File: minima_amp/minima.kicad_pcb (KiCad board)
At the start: 2 copper layers, 78 x 60 mm, 40 parts, among them J1 input, J2 output, J3 powersupply, U1 LM1875

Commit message: Minor PCB adjustements
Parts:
- moved J1 0.64 mm to (120.6, 97.7)
- moved J3 0.08 mm to (140.6, 99.8)
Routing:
- net VCC: track 50.4 -> 46.4 mm
- net GNDPWR: track 106.8 -> 102.9 mm
- net VEE: track 53.5 -> 49.6 mm
- net /inp: track 13.4 -> 12.5 mm
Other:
- board text added: "180801"
- board text added: "Grid alignements: - Components: PIN3 (U1) 25mil - Planes: PIN4 (U1) 10mil - Connectors: LEFT-UP Corner 1mm"
- board text removed: "20180801"

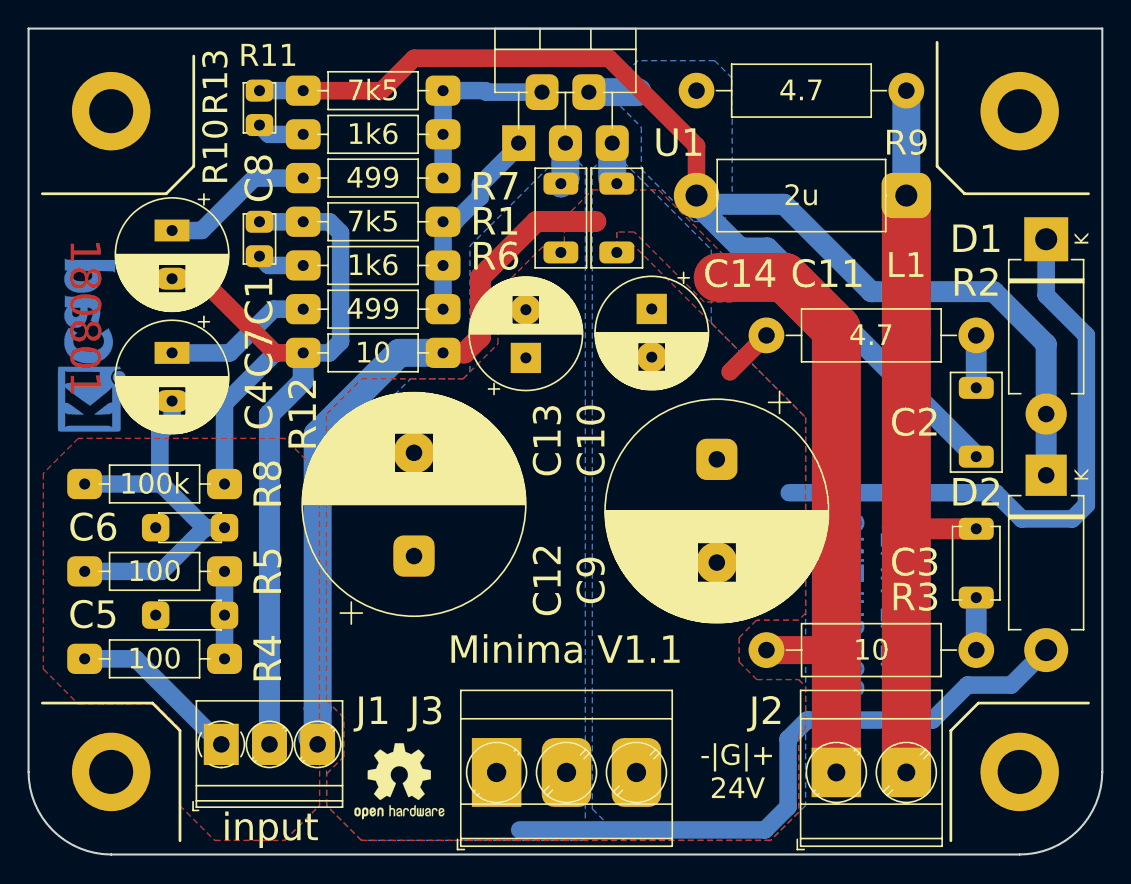
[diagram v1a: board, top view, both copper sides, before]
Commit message: Using designators as specified in README.rst
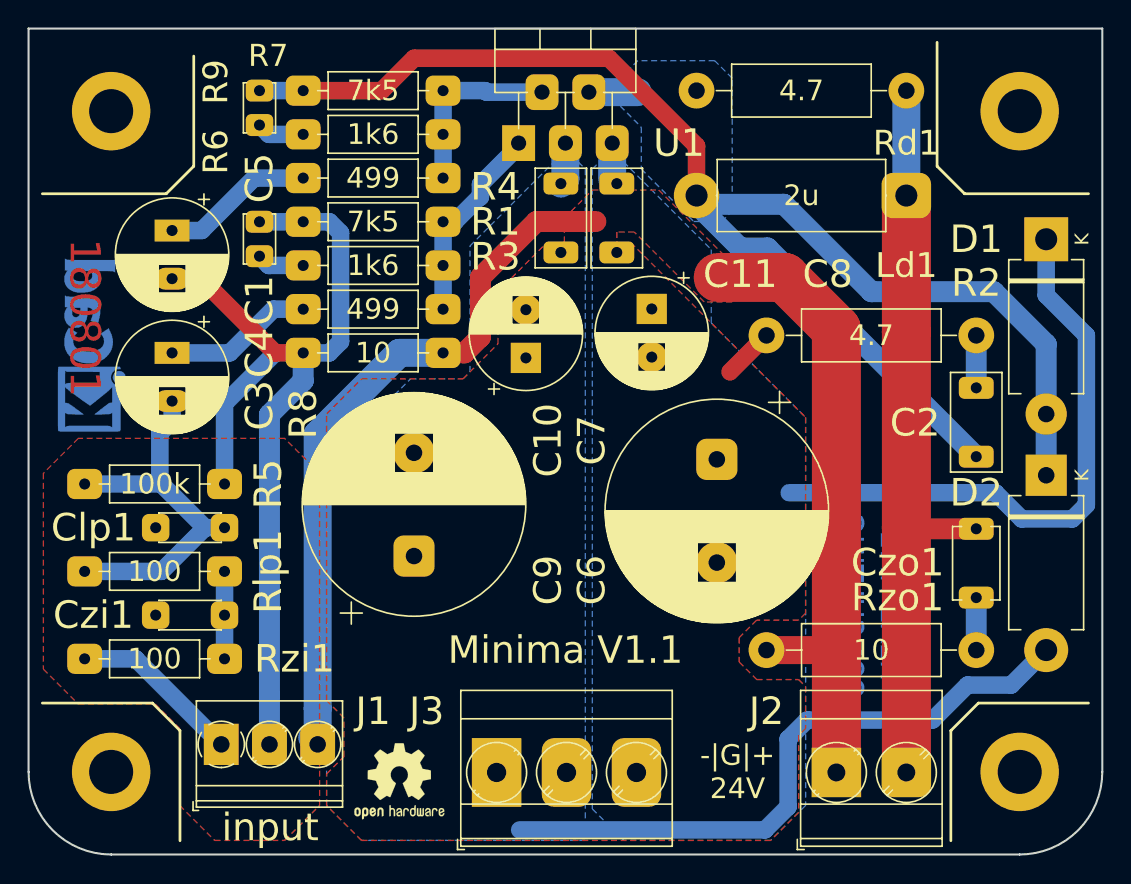
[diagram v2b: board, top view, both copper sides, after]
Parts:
- renumbered C13 to C10, C14 to C11, C4 to C3, C7 to C4, C8 to C5, C9 to C6, C10 to C7, C11 to C8, C12 to C9, C6 to Clp1, C5 to Czi1, C3 to Czo1, L1 to Ld1, R6 to R3, R7 to R4, R8 to R5, R10 to R6, R11 to R7, R12 to R8, R13 to R9, R9 to Rd1, R5 to Rlp1, R4 to Rzi1, R3 to Rzo1

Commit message: Using Pluggable Terminal Block
Signed-off-by: Nenad Radulovic <nenad.b.radulovic@gmail.com>
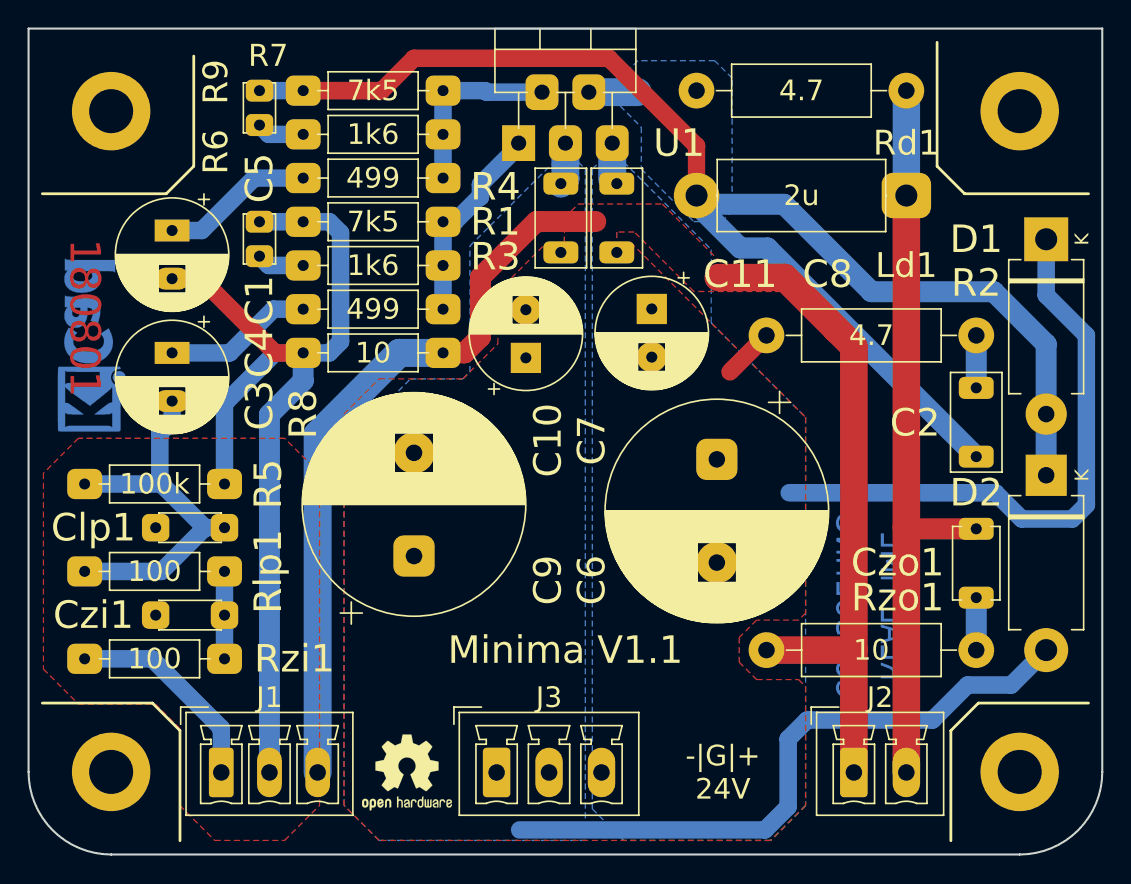
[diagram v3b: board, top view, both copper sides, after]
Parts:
- J1: footprint TerminalBlock_Phoenix:TerminalBlock_Phoenix_PT-1,5-3-3.5-H_1x03_P3.50mm_Horizontal -> Connector_Phoenix_MC:PhoenixContact_MCV_1,5_3-G-3.5_1x03_P3.50mm_Vertical
- J2: footprint TerminalBlock_Phoenix:TerminalBlock_Phoenix_MKDS-3-2-5.08_1x02_P5.08mm_Horizontal -> Connector_Phoenix_MC:PhoenixContact_MCV_1,5_2-G-3.81_1x02_P3.81mm_Vertical
- J3: footprint TerminalBlock_Phoenix:TerminalBlock_Phoenix_MKDS-3-3-5.08_1x03_P5.08mm_Horizontal -> Connector_Phoenix_MC:PhoenixContact_MCV_1,5_3-G-3.81_1x03_P3.81mm_Vertical
- moved J1 2.04 mm to (120.6, 99.8)
- moved J2 1.27 mm to (166.5, 99.8)
- moved LOGO2 0.84 mm to (134.1, 99.8)
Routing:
- net GNDPWR: track 102.9 -> 106.7 mm
- net /inp: track 12.5 -> 15.2 mm
- net /sgnd: track 71.5 -> 73.5 mm
- net /spkhot: track 54.6 -> 54.0 mm
